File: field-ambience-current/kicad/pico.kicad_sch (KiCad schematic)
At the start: 9 parts, among them J4 SWD 1.27mm (SWCLK/GND/SWDIO), SW11 Reset 6mm SMD, SW12 BOOTSEL 6mm SMD (DNP for THT-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, U1 Raspberry_Pi_Pico2 (RP2350)

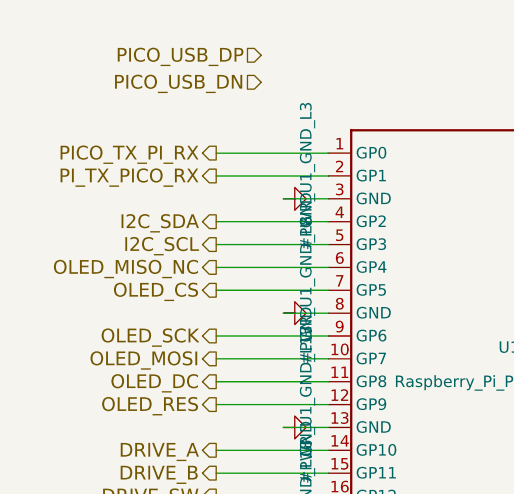
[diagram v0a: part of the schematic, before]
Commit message: feat(native): Step 6 — Pi removed from schematic + BOM (97→92 parts)
Now that the RP2350 owns display, buttons, encoders, and I²S audio
(Steps 1-5), the Raspberry Pi Zero 2 W comes out of the device.

generate_kicad_project.py:
- Deleted pi.kicad_sch (Sheet 7, Pi header); removed it from the kicad_pro
  sheet list, the root sheet hierarchy, and main()'s writer.
- 5 components removed: J2 (40-pin Pi header), R1 (UART RX series),
  R_BCK/R_LRCK/R_DOUT (Pi-side I²S series Rs). Real component count 97→92.
- pico_sheet: GP0/GP1/GP4 repurposed from UART TX/RX + unused OLED MISO
  to I2S_BCK / I2S_LRCK / I2S_DOUT (RP2350 PIO I²S master). Fixed a
  pin-number vs GP-number slip so I2C_SDA/SCL stay on pins 4/5.
- root_sheet: Pico symbol's 2 UART pins replaced with 3 I²S output pins;
  UART + Pi-side label bridges removed; new Pico-I²S→Audio label bridges
  added (audio-side I²S labels were already present, now Pico-driven).
- D2 (TVS) kept: it sits on the +5V main rail, not the Pi header — stays
  as general rail surge protection.

Verification:
- Regenerates clean; pi.kicad_sch not recreated; all sheets paren-balanced.
- Removed nets (PICO_TX_PI_RX/PI_TX_PICO_RX/OLED_MISO_NC) gone everywhere.
- I²S nets continuous pico→root→audio; every pico hier-label has a root pin
  (only ADC_VREF_NC unmatched — pre-existing intentional NC).
- kicad-happy analyzer: 6 VM-001 blockers, ALL the documented false-positive
  class (Pico VBUS pin makes the heuristic treat GPIOs as 5V; real I²S is
  GP0/1/4 @ 3V3 → PCM5102A @ 3V3, no level shifter needed). Warnings 19→16.
  GUI ERC (B3) remains the authority.

Docs: SPEC §5 pin rows + v0.9 banner, CHANGELOG v0.9, MEINE_TODO Abschnitt 0,
NATIVE_PORT_PLAN Step 6 ticked + D2 correction. pi_sheet() left as dead code
(uncalled) to keep the diff focused.

https://claude.ai/code/session_01K5kLTFpDCCoYwx2dq6RkAv
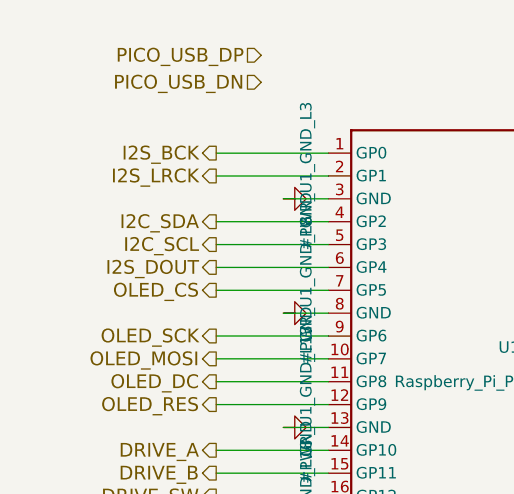
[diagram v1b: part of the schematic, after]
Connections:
- net OLED_MISO_NC renamed I2S_DOUT
- net PICO_TX_PI_RX renamed I2S_BCK
- net PI_TX_PICO_RX renamed I2S_LRCK
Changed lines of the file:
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@@
     (effects (font (size 1.524 1.524)) (justify right))
 )
-  (hierarchical_label "PICO_TX_PI_RX" (shape output) (at 70 75.87 0)
+  (hierarchical_label "I2S_BCK" (shape output) (at 70 75.87 0)
     (effects (font (size 1.524 1.524)) (justify right))
 )
-  (hierarchical_label "PI_TX_PICO_RX" (shape output) (at 70 78.41000000000001 0)
+  (hierarchical_label "I2S_LRCK" (shape output) (at 70 78.41000000000001 0)
     (effects (font (size 1.524 1.524)) (justify right))
 )
@@
     (effects (font (size 1.524 1.524)) (justify right))
 )
-  (hierarchical_label "OLED_MISO_NC" (shape output) (at 70 88.57000000000001 0)
+  (hierarchical_label "I2S_DOUT" (shape output) (at 70 88.57000000000001 0)
     (effects (font (size 1.524 1.524)) (justify right))
 )
